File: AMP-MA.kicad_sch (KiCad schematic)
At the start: 30 parts, among them Q1 2N5484, Q12 2N5484, Q13 2N5484, Q2 2N5484

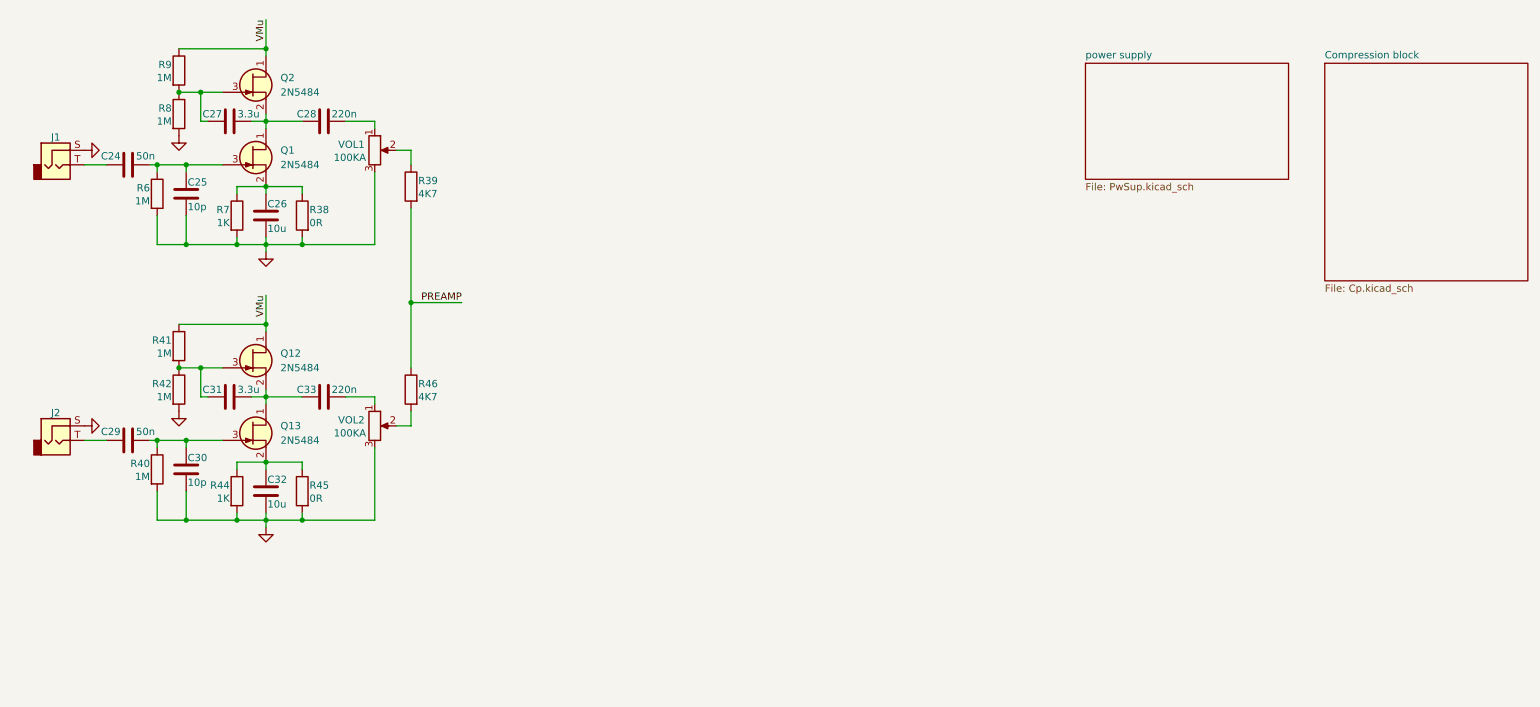
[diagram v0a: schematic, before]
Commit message: Schem & Lib upd
Lib: added footprint and Symbol foe new 6pin jack    Schem: changed jacks
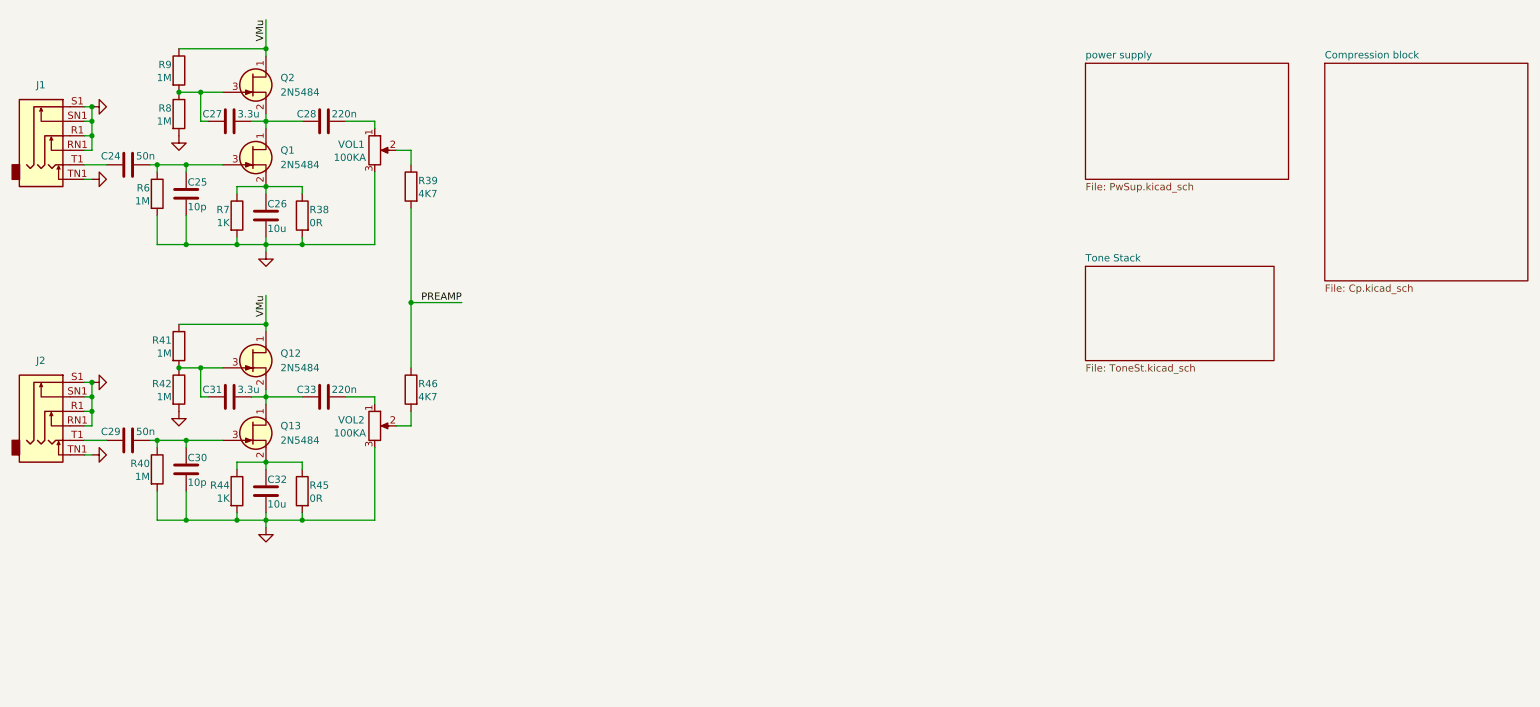
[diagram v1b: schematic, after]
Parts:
- removed J1, J2: (no value), symbol PrLib:Audio_Jack
- added J1, J2: (no value), PrLib:Jack_3_6pin, symbol PrLib:Audio_Jack_3
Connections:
- net GND: now also J1.R1, J1.RN1, J1.S1, J1.SN1, J1.TN1, J2.R1, J2.RN1, J2.S1, J2.SN1, J2.TN1
- net at C29.1: now also J2.T1
- net at C24.1: now also J1.T1
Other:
- added sheet Tone Stack (ToneSt.kicad_sch)

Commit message: Schem upd
Tone Stack addded
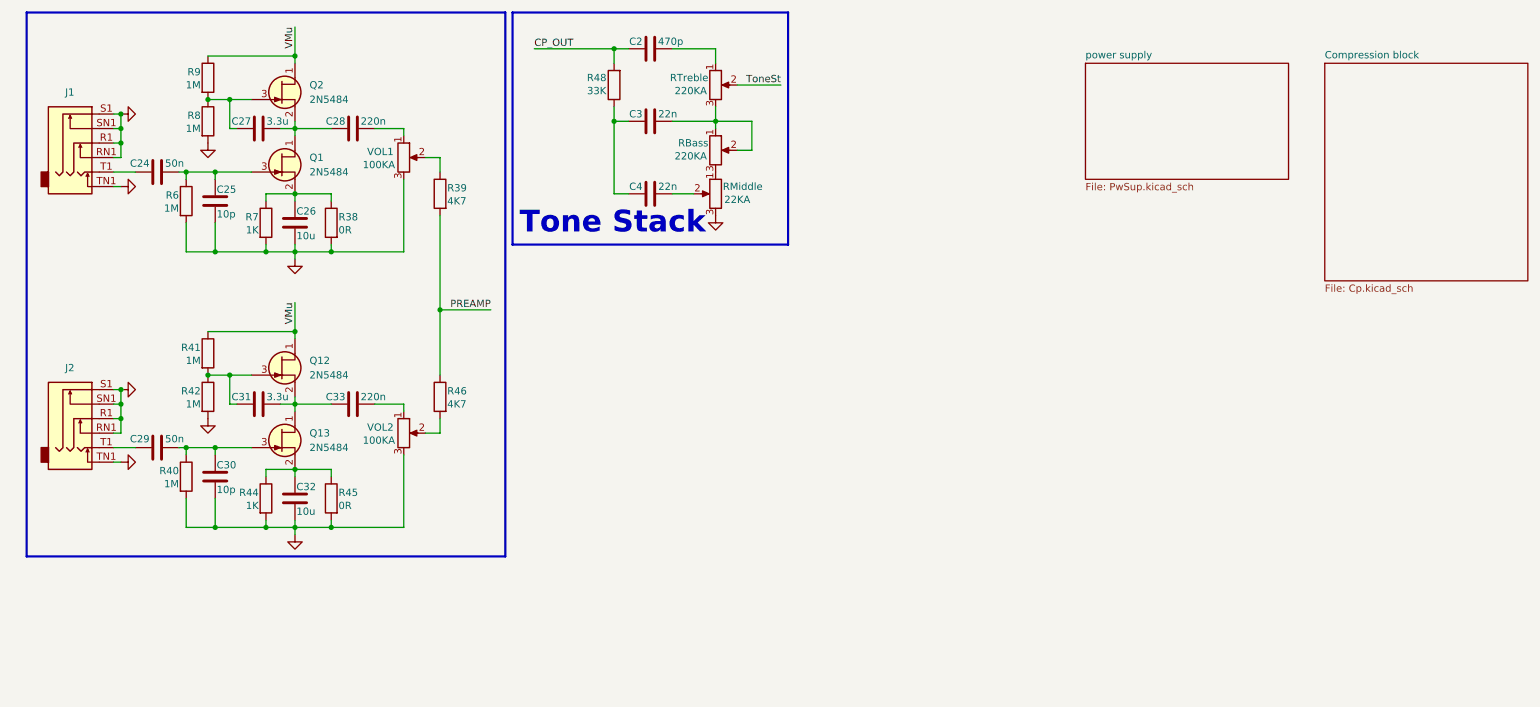
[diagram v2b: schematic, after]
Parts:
- added C2: 470p, symbol Device:C
- added C3, C4: 22n, symbol Device:C
- added R48: 33K, symbol Device:R
- added RBass, RTreble: 220KA, symbol Device:R_Potentiometer
- added RMiddle: 22KA, symbol Device:R_Potentiometer
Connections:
- net GND: now also RMiddle.3
- new net: C3.1, C4.1, R48.1
- new net: C3.2, RBass.1, RBass.2, RTreble.3
- new net: C4.2, RMiddle.2
- new net: C2.2, RTreble.1
- new net: RBass.3, RMiddle.1
- new net CP_OUT: C2.1, R48.2
- new net ToneSt: RTreble.2
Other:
- removed sheet Tone Stack
- note added: "Tone Stack"
- moved on the sheet: C24, C25, C26, C27, C28, C29, C30, C31, C32, C33, J1, J2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

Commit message: Schem & README upd
added AMP block
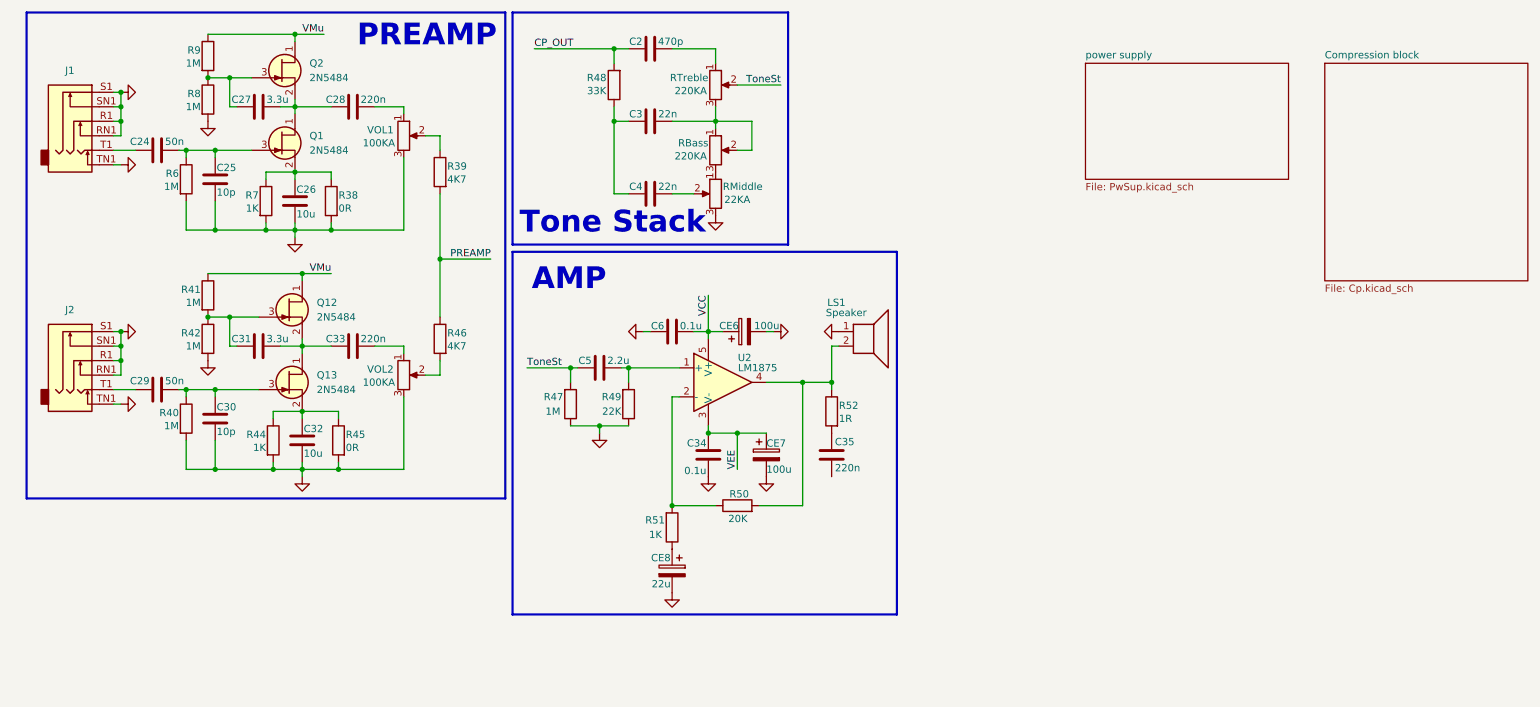
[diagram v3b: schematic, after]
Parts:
- added C34, C6: 0.1u, symbol Device:C
- added C35: 220n, symbol Device:C
- added C5: 2.2u, symbol Device:C
- added CE6, CE7: 100u, Capacitor_THT:CP_Radial_D6.3mm_P2.50mm, symbol Device:C_Polarized
- added CE8: 22u, Capacitor_THT:CP_Radial_D5.0mm_P2.50mm, symbol Device:C_Polarized
- added LS1: Speaker, symbol Device:Speaker
- added R47: 1M, symbol Device:R
- added R49: 22K, symbol Device:R
- added R50: 20K, symbol Device:R
- added R51: 1K, symbol Device:R
- added R52: 1R, symbol Device:R
- added U2: LM1875, Package_TO_SOT_THT:TO-220-5_P3.4x3.7mm_StaggerOdd_Lead3.8mm_Vertical, symbol Amplifier_Audio:LM1875
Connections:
- net GND: now also C34.2, C6.1, CE6.2, CE7.2, CE8.2, LS1.1, R47.1, R49.1
- net ToneSt: now also C5.1, R47.2
- new net: LS1.2, R50.2, R52.1, U2.4
- new net: C35.1, R52.2
- new net: CE8.1, R51.1
- new net: R50.1, R51.2, U2.2 (-)
- new net: C5.2, R49.2, U2.1 (+)
- new net VCC: C6.2, CE6.1, U2.5 (V+)
- new net VEE: C34.1, CE7.1, U2.3 (V-)
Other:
- note added: "AMP"
- note added: "PREAMP"
- moved on the sheet: C24, C25, C26, C27, C28, C29, C30, C31, C32, C33, J1, J2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

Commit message: Big upd
moved hierarical Sheets to direсtory Schematics, revorked power supply
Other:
- sheet Compression block: file Cp.kicad_sch -> Schematics/Cp.kicad_sch
- sheet power supply: file PwSup.kicad_sch -> Schematics/PwSup.kicad_sch
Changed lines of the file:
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@@
 			)
 		)
-		(property "Sheetfile" "PwSup.kicad_sch"
+		(property "Sheetfile" "Schematics/PwSup.kicad_sch"
 			(at 198.12 42.4946 0)
 			(show_name no)
@@
 			(project "AMP-MA"
 				(path "/4094031b-a9da-4ac5-aaa1-42b342c92a3e"
-					(page "3")
+					(page "2")
 				)
 			)
@@
 			)
 		)
-		(property "Sheetfile" "Cp.kicad_sch"
+		(property "Sheetfile" "Schematics/Cp.kicad_sch"
 			(at 240.03 60.2746 0)
 			(show_name no)
@@
 			(project "AMP-MA"
 				(path "/4094031b-a9da-4ac5-aaa1-42b342c92a3e"
-					(page "2")
+					(page "3")
 				)
 			)

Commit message: footprints assigned
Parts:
- C2, C24, C25, C26, C27, C28, C29, C3, C30, C31, C32, C33, C34, C35, C4, C5, C6: footprint (none) -> Capacitor_THT:C_Disc_D7.0mm_W2.5mm_P5.00mm
- LS1: footprint (none) -> Connector_PinSocket_2.54mm:PinSocket_1x02_P2.54mm_Vertical
- Q1, Q12, Q13, Q2: footprint PCM_Package_TO_SOT_THT_AKL:TO-92_Inline_Wide_DSG -> Package_TO_SOT_THT:TO-92_Inline
- R38, R39, R40, R41, R42, R44, R45, R46, R47, R48, R49, R50, R51, R52, R6, R7, R8, R9: footprint (none) -> Resistor_THT:R_Axial_DIN0207_L6.3mm_D2.5mm_P10.16mm_Horizontal
- RBass1: renamed from RBass; footprint (none) -> Potentiometer_THT:Potentiometer_Vishay_248BH-249BH_Single_Horizontal
- RMiddle1: renamed from RMiddle; footprint (none) -> Potentiometer_THT:Potentiometer_Vishay_248BH-249BH_Single_Horizontal
- RTreble1: renamed from RTreble; footprint (none) -> Potentiometer_THT:Potentiometer_Vishay_248BH-249BH_Single_Horizontal
- VOL1, VOL2: footprint (none) -> Potentiometer_THT:Potentiometer_Vishay_248BH-249BH_Single_Horizontal
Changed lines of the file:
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@@
 	)
 	(junction
+		(at 125.73 99.06)
+		(diameter 0)
+		(color 0 0 0 0)
+	)
+	(junction
 		(at 29.21 68.58)
 		(diameter 0)
@@
 		(color 0 0 0 0)
 	)
-	(junction
-		(at 125.73 99.06)
-		(diameter 0)
-		(color 0 0 0 0)
-	)
 	(wire
 		(pts
@@
 			)
 		)
-		(property "Footprint" ""
+		(property "Footprint" "Potentiometer_THT:Potentiometer_Vishay_248BH-249BH_Single_Horizontal"
 			(at 78.74 34.29 0)
 			(hide yes)
@@
 			)
 		)
-		(property "Footprint" ""
+		(property "Footprint" "Resistor_THT:R_Axial_DIN0207_L6.3mm_D2.5mm_P10.16mm_Horizontal"
 			(at 42.672 20.32 90)
 			(hide yes)
@@
 			)
 		)
-		(property "Footprint" ""
+		(property "Footprint" "Resistor_THT:R_Axial_DIN0207_L6.3mm_D2.5mm_P10.16mm_Horizontal"
 			(at 86.868 69.85 90)
 			(hide yes)
@@
 			)
 		)
-		(property "Footprint" ""
+		(property "Footprint" "Resistor_THT:R_Axial_DIN0207_L6.3mm_D2.5mm_P10.16mm_Horizontal"
 			(at 106.172 81.28 90)
 			(hide yes)
@@
 			)
 		)
-		(property "Footprint" ""
+		(property "Footprint" "Capacitor_THT:C_Disc_D7.0mm_W2.5mm_P5.00mm"
 			(at 125.73 30.7848 0)
 			(hide yes)
@@
 			)
 		)
-		(property "Footprint" ""
+		(property "Footprint" "Capacitor_THT:C_Disc_D7.0mm_W2.5mm_P5.00mm"
 			(at 44.7548 80.01 0)
 			(hide yes)
@@
 			)
 		)
-		(property "Footprint" ""
+		(property "Footprint" "Resistor_THT:R_Axial_DIN0207_L6.3mm_D2.5mm_P10.16mm_Horizontal"
 			(at 155.448 82.55 90)
 			(hide yes)
@@
 			)
 		)
-		(property "Footprint" ""
+		(property "Footprint" "Capacitor_THT:C_Disc_D7.0mm_W2.5mm_P5.00mm"
 			(at 39.37 77.7748 0)
 			(hide yes)
@@
 			)
 		)
-		(property "Footprint" ""
+		(property "Footprint" "Capacitor_THT:C_Disc_D7.0mm_W2.5mm_P5.00mm"
 			(at 125.73 43.4848 0)
 			(hide yes)
@@
 			)
 		)
-		(property "Footprint" ""
+		(property "Footprint" "Resistor_THT:R_Axial_DIN0207_L6.3mm_D2.5mm_P10.16mm_Horizontal"
 			(at 38.862 41.91 90)
 			(hide yes)
@@
 			)
 		)
-		(property "Footprint" "PCM_Package_TO_SOT_THT_AKL:TO-92_Inline_Wide_DSG"
+		(property "Footprint" "Package_TO_SOT_THT:TO-92_Inline"
 			(at 63.5 74.93 0)
 			(hide yes)
@@
 			)
 		)
-		(property "Footprint" ""
+		(property "Footprint" "Capacitor_THT:C_Disc_D7.0mm_W2.5mm_P5.00mm"
 			(at 57.15 28.2448 0)
 			(hide yes)
@@
 			)
 		)
-		(property "Footprint" ""
+		(property "Footprint" "Capacitor_THT:C_Disc_D7.0mm_W2.5mm_P5.00mm"
 			(at 59.9948 83.82 0)
 			(hide yes)
@@
 			)
 		)
-		(property "Footprint" ""
+		(property "Footprint" "Capacitor_THT:C_Disc_D7.0mm_W2.5mm_P5.00mm"
 			(at 129.54 67.6148 0)
 			(hide yes)
@@
 			)
 		)
-		(property "Footprint" ""
+		(property "Footprint" "Capacitor_THT:C_Disc_D7.0mm_W2.5mm_P5.00mm"
 			(at 44.7548 38.1 0)
 			(hide yes)
@@
 			)
 		)
-		(property "Footprint" ""
+		(property "Footprint" "Capacitor_THT:C_Disc_D7.0mm_W2.5mm_P5.00mm"
 			(at 39.37 35.8648 0)
 			(hide yes)
@@
 			)
 		)
-		(property "Footprint" ""
+		(property "Footprint" "Potentiometer_THT:Potentiometer_Vishay_248BH-249BH_Single_Horizontal"
 			(at 78.74 76.2 0)
 			(hide yes)
@@
 			)
 		)
-		(property "Footprint" ""
+		(property "Footprint" "Capacitor_THT:C_Disc_D7.0mm_W2.5mm_P5.00mm"
 			(at 58.7248 41.91 0)
 			(hide yes)
@@
 			)
 		)
-		(property "Footprint" ""
+		(property "Footprint" "Resistor_THT:R_Axial_DIN0207_L6.3mm_D2.5mm_P10.16mm_Horizontal"
 			(at 67.818 45.72 90)
 			(hide yes)
@@
 			)
 		)
-		(property "Footprint" ""
+		(property "Footprint" "Resistor_THT:R_Axial_DIN0207_L6.3mm_D2.5mm_P10.16mm_Horizontal"
 			(at 69.088 87.63 90)
 			(hide yes)
@@
 			)
 		)
-		(property "Footprint" ""
+		(property "Footprint" "Resistor_THT:R_Axial_DIN0207_L6.3mm_D2.5mm_P10.16mm_Horizontal"
 			(at 137.16 100.838 90)
 			(hide yes)
@@
 			)
 		)
-		(property "Footprint" ""
+		(property "Footprint" "Resistor_THT:R_Axial_DIN0207_L6.3mm_D2.5mm_P10.16mm_Horizontal"
 			(at 52.832 45.72 90)
 			(hide yes)
@@
 			)
 		)
-		(property "Footprint" ""
+		(property "Footprint" "Resistor_THT:R_Axial_DIN0207_L6.3mm_D2.5mm_P10.16mm_Horizontal"
 			(at 54.102 87.63 90)
 			(hide yes)
@@
 			)
 		)
-		(property "Footprint" ""
+		(property "Footprint" "Resistor_THT:R_Axial_DIN0207_L6.3mm_D2.5mm_P10.16mm_Horizontal"
 			(at 117.348 25.4 90)
 			(hide yes)
@@
 			)
 		)
-		(property "Footprint" ""
+		(property "Footprint" "Capacitor_THT:C_Disc_D7.0mm_W2.5mm_P5.00mm"
 			(at 125.73 18.0848 0)
 			(hide yes)
@@
 			)
 		)
-		(property "Footprint" ""
+		(property "Footprint" "Resistor_THT:R_Axial_DIN0207_L6.3mm_D2.5mm_P10.16mm_Horizontal"
 			(at 116.332 81.28 90)
 			(hide yes)
@@
 			)
 		)
-		(property "Footprint" ""
+		(property "Footprint" "Resistor_THT:R_Axial_DIN0207_L6.3mm_D2.5mm_P10.16mm_Horizontal"
 			(at 86.868 40.64 90)
 			(hide yes)
@@
 			)
 		)
-		(property "Footprint" ""
+		(property "Footprint" "Capacitor_THT:C_Disc_D7.0mm_W2.5mm_P5.00mm"
 			(at 154.6352 93.98 0)
 			(hide yes)
@@
 			)
 		)
-		(property "Footprint" ""
+		(property "Footprint" "Resistor_THT:R_Axial_DIN0207_L6.3mm_D2.5mm_P10.16mm_Horizontal"
 			(at 42.672 27.94 90)
 			(hide yes)
@@
 			)
 		)
-		(property "Footprint" ""
+		(property "Footprint" "Capacitor_THT:C_Disc_D7.0mm_W2.5mm_P5.00mm"
 			(at 131.1148 93.98 0)
 			(hide yes)
@@
 			)
 		)
-		(property "Footprint" ""
+		(property "Footprint" "Resistor_THT:R_Axial_DIN0207_L6.3mm_D2.5mm_P10.16mm_Horizontal"
 			(at 38.862 83.82 90)
 			(hide yes)
@@
 			)
 		)
-		(property "Footprint" "PCM_Package_TO_SOT_THT_AKL:TO-92_Inline_Wide_DSG"
+		(property "Footprint" "Package_TO_SOT_THT:TO-92_Inline"
 			(at 62.23 20.32 0)
 			(hide yes)
@@
 			)
 		)
-		(property "Footprint" "PCM_Package_TO_SOT_THT_AKL:TO-92_Inline_Wide_DSG"
+		(property "Footprint" "Package_TO_SOT_THT:TO-92_Inline"
 			(at 62.23 33.02 0)
 			(hide yes)
@@
 			)
 		)
-		(property "Footprint" ""
+		(property "Footprint" "Capacitor_THT:C_Disc_D7.0mm_W2.5mm_P5.00mm"
 			(at 57.15 70.1548 0)
 			(hide yes)
@@
 			)
 		)
-		(property "Footprint" ""
+		(property "Footprint" "Resistor_THT:R_Axial_DIN0207_L6.3mm_D2.5mm_P10.16mm_Horizontal"
 			(at 42.672 69.85 90)
 			(hide yes)
@@
 		(in_pos_files yes)
 		(dnp no)
-		(property "Reference" "RBass"
+		(property "Reference" "RBass1"
 			(at 132.08 35.56 0)
 			(show_name no)
@@
 			)
 		)
-		(property "Footprint" ""
+		(property "Footprint" "Potentiometer_THT:Potentiometer_Vishay_248BH-249BH_Single_Horizontal"
 			(at 133.35 36.83 0)
 			(hide yes)
@@
 			(project "AMP-MA"
 				(path "/4094031b-a9da-4ac5-aaa1-42b342c92a3e"
-					(reference "RBass")
+					(reference "RBass1")
 					(unit 1)
 				)
@@
 			)
 		)
-		(property "Footprint" ""
+		(property "Footprint" "Capacitor_THT:C_Disc_D7.0mm_W2.5mm_P5.00mm"
 			(at 116.84 73.9648 0)
 			(hide yes)
@@
 			)
 		)
-		(property "Footprint" ""
+		(property "Footprint" "Connector_PinSocket_2.54mm:PinSocket_1x02_P2.54mm_Vertical"
 			(at 160.02 73.66 0)
 			(hide yes)
@@
 		(in_pos_files yes)
 		(dnp no)
-		(property "Reference" "RTreble"
+		(property "Reference" "RTreble1"
 			(at 132.08 24.13 0)
 			(show_name no)
@@
 			)
 		)
-		(property "Footprint" ""
+		(property "Footprint" "Potentiometer_THT:Potentiometer_Vishay_248BH-249BH_Single_Horizontal"
 			(at 133.35 25.4 0)
 			(hide yes)
@@
 			(project "AMP-MA"
 				(path "/4094031b-a9da-4ac5-aaa1-42b342c92a3e"
-					(reference "RTreble")
+					(reference "RTreble1")
 					(unit 1)
 				)
@@
 			)
 		)
-		(property "Footprint" ""
+		(property "Footprint" "Resistor_THT:R_Axial_DIN0207_L6.3mm_D2.5mm_P10.16mm_Horizontal"
 			(at 42.672 62.23 90)
 			(hide yes)
@@
 		(in_pos_files yes)
 		(dnp no)
-		(property "Reference" "RMiddle"
+		(property "Reference" "RMiddle1"
 			(at 134.62 43.18 0)
 			(show_name no)
@@
 			)
 		)
-		(property "Footprint" ""
+		(property "Footprint" "Potentiometer_THT:Potentiometer_Vishay_248BH-249BH_Single_Horizontal"
 			(at 133.35 44.45 0)
 			(hide yes)
@@
 			(project "AMP-MA"
 				(path "/4094031b-a9da-4ac5-aaa1-42b342c92a3e"
-					(reference "RMiddle")
+					(reference "RMiddle1")
 					(unit 1)
 				)
@@
 			)
 		)
-		(property "Footprint" ""
+		(property "Footprint" "Capacitor_THT:C_Disc_D7.0mm_W2.5mm_P5.00mm"
 			(at 73.66 28.2448 0)
 			(hide yes)
@@
 			)
 		)
-		(property "Footprint" "PCM_Package_TO_SOT_THT_AKL:TO-92_Inline_Wide_DSG"
+		(property "Footprint" "Package_TO_SOT_THT:TO-92_Inline"
 			(at 63.5 62.23 0)
 			(hide yes)
@@
 			)
 		)
-		(property "Footprint" ""
+		(property "Footprint" "Capacitor_THT:C_Disc_D7.0mm_W2.5mm_P5.00mm"
 			(at 73.66 70.1548 0)
 			(hide yes)
@@
 			)
 		)
-		(property "Footprint" ""
+		(property "Footprint" "Resistor_THT:R_Axial_DIN0207_L6.3mm_D2.5mm_P10.16mm_Horizontal"
 			(at 123.952 102.87 90)
 			(hide yes)
